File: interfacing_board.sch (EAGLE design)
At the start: 67 parts, among them IC1 MAX3096CSE, IC2 MAX3096CSE, X1 87758-3816, X2 87758-3816

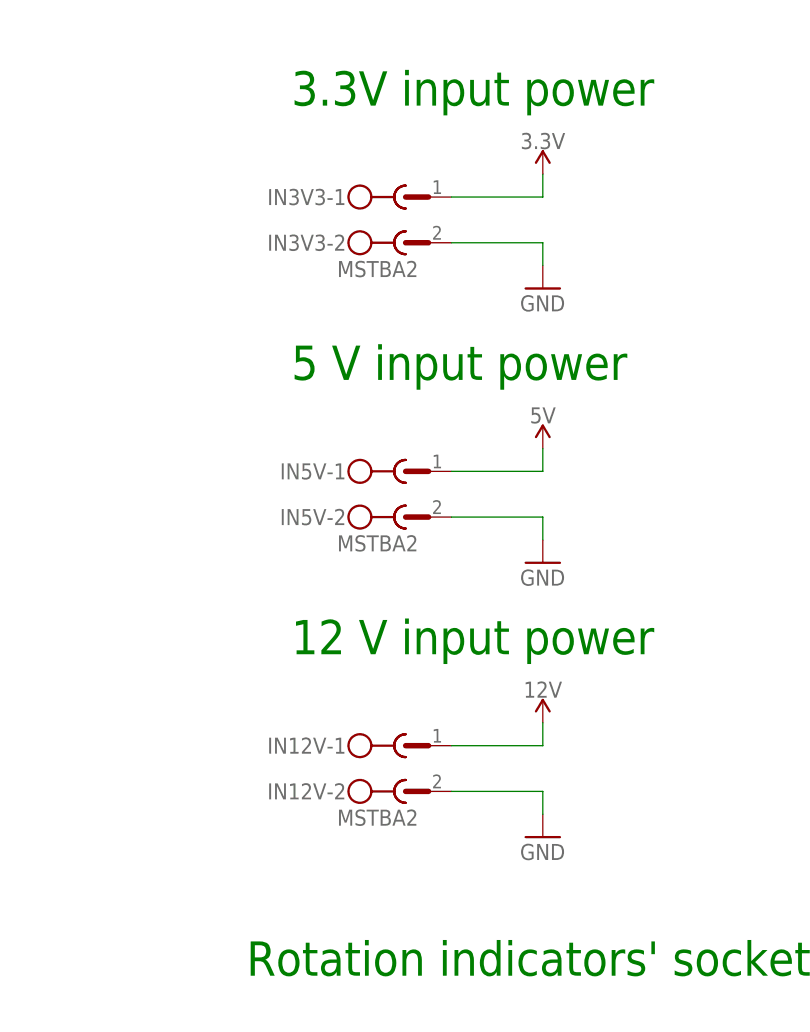
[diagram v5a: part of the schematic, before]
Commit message: Changed connector in bipop_power_supply board, modified routing and board's dimensions.
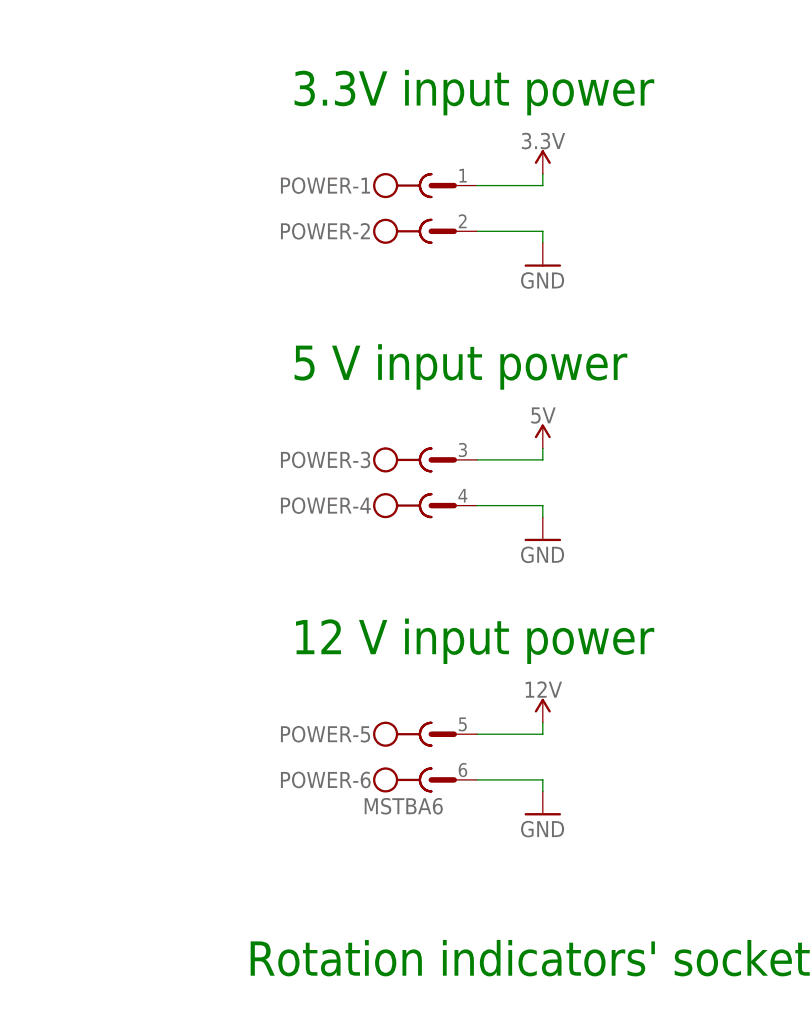
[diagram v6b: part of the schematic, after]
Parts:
- removed IN12V, IN3V3, IN5V: MSTBA2, con-phoenix-508:MSTBA2
- added POWER: MSTBA6, con-phoenix-508:MSTBA6
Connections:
- net 12V: now also POWER-5.1; no longer IN12V-1.1
- net 3.3V: now also POWER-1.1; no longer IN3V3-1.1
- net 5V: now also POWER-3.1; no longer IN5V-1.1
- net GND: now also POWER-2.1, POWER-4.1, POWER-6.1; no longer IN12V-2.1, IN3V3-2.1, IN5V-2.1
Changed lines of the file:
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@@
 <setting verticaltext="up"/>
 </settings>
-<grid distance="0.1" unitdist="inch" unit="inch" style="lines" multiple="1" display="no" altdistance="0.01" altunitdist="inch" altunit="inch"/>
+<grid distance="0.1" unitdist="inch" unit="inch" style="lines" multiple="1" display="yes" altdistance="0.01" altunitdist="inch" altunit="inch"/>
 <layers>
 <layer number="1" name="Top" color="4" fill="10" visible="no" active="no"/>
@@
 <part name="GND8" library="supply1" library_urn="urn:adsk.eagle:library:371" deviceset="GND" device=""/>
 <part name="ETHER" library="con-garry" library_urn="urn:adsk.eagle:library:147" deviceset="332-10" device="" package3d_urn="urn:adsk.eagle:package:6812/1"/>
-<part name="IN12V" library="con-phoenix-508" library_urn="urn:adsk.eagle:library:176" deviceset="MSTBA2" device="" package3d_urn="urn:adsk.eagle:package:9615/1"/>
-<part name="IN3V3" library="con-phoenix-508" library_urn="urn:adsk.eagle:library:176" deviceset="MSTBA2" device="" package3d_urn="urn:adsk.eagle:package:9615/1"/>
 <part name="GND21" library="supply1" library_urn="urn:adsk.eagle:library:371" deviceset="GND" device=""/>
 <part name="SUPPLY15" library="SparkFun-PowerSymbols" library_urn="urn:adsk.eagle:library:530" deviceset="12V" device=""/>
@@
 <part name="SUPPLY39" library="SparkFun-PowerSymbols" library_urn="urn:adsk.eagle:library:530" deviceset="3.3V" device=""/>
 <part name="GND4" library="supply1" library_urn="urn:adsk.eagle:library:371" deviceset="GND" device=""/>
-<part name="IN5V" library="con-phoenix-508" library_urn="urn:adsk.eagle:library:176" deviceset="MSTBA2" device="" package3d_urn="urn:adsk.eagle:package:9615/1"/>
 <part name="SUPPLY24" library="SparkFun-PowerSymbols" library_urn="urn:adsk.eagle:library:530" deviceset="3.3V" device=""/>
 <part name="GND39" library="supply1" library_urn="urn:adsk.eagle:library:371" deviceset="GND" device=""/>
@@
 <part name="GND31" library="SparkFun-PowerSymbols" library_urn="urn:adsk.eagle:library:530" deviceset="GND" device=""/>
 <part name="GND32" library="SparkFun-PowerSymbols" library_urn="urn:adsk.eagle:library:530" deviceset="GND" device=""/>
+<part name="POWER" library="con-phoenix-508" library_urn="urn:adsk.eagle:library:176" deviceset="MSTBA6" device="" package3d_urn="urn:adsk.eagle:package:9616/1"/>
 </parts>
 <sheets>
@@
 <instance part="X2" gate="-37" x="-18.44" y="179.42" rot="R180"/>
 <instance part="X2" gate="-38" x="-43.84" y="179.42" rot="MR180"/>
-<instance part="GND2" gate="1" x="-15.552978125" y="-118.11301875"/>
+<instance part="GND2" gate="1" x="-15.552978125" y="-115.57301875"/>
 <instance part="GND3" gate="1" x="63.027021875" y="-172.39301875"/>
 <instance part="SUPPLY2" gate="G$1" x="63.027021875" y="-164.69301875"/>
@@
 <instance part="ETHER" gate="-9" x="84.007021875" y="-122.59301875" rot="MR0"/>
 <instance part="ETHER" gate="-10" x="53.527021875" y="-122.59301875"/>
-<instance part="IN12V" gate="-1" x="-30.792978125" y="-168.91301875"/>
-<instance part="IN12V" gate="-2" x="-30.792978125" y="-173.99301875"/>
-<instance part="IN3V3" gate="-1" x="-30.792978125" y="-107.95301875"/>
-<instance part="IN3V3" gate="-2" x="-30.792978125" y="-113.03301875"/>
-<instance part="GND21" gate="1" x="-15.552978125" y="-179.07301875"/>
+<instance part="GND21" gate="1" x="-15.552978125" y="-176.53301875"/>
 <instance part="SUPPLY15" gate="G$1" x="-15.552978125" y="-166.37301875"/>
 <instance part="SUPPLY1" gate="G$1" x="-15.552978125" y="-105.41301875"/>
@@
 <instance part="R18" gate="G$1" x="82.528246875" y="-388.03574375" rot="R90"/>
 <instance part="SUPPLY39" gate="G$1" x="82.528246875" y="-382.95574375"/>
-<instance part="GND4" gate="1" x="-15.552978125" y="-148.59301875"/>
-<instance part="IN5V" gate="-1" x="-30.792978125" y="-138.43301875"/>
-<instance part="IN5V" gate="-2" x="-30.792978125" y="-143.51301875"/>
+<instance part="GND4" gate="1" x="-15.552978125" y="-146.05301875"/>
 <instance part="SUPPLY24" gate="G$1" x="52.048246875" y="-382.95574375"/>
 <instance part="GND39" gate="1" x="52.048246875" y="-403.27574375"/>
@@
 <instance part="GND31" gate="1" x="7.62" y="210.82"/>
 <instance part="GND32" gate="1" x="7.62" y="226.06"/>
+<instance part="POWER" gate="-1" x="-27.94" y="-106.68"/>
+<instance part="POWER" gate="-2" x="-27.94" y="-111.76"/>
+<instance part="POWER" gate="-3" x="-27.94" y="-137.16"/>
+<instance part="POWER" gate="-4" x="-27.94" y="-142.24"/>
+<instance part="POWER" gate="-5" x="-27.94" y="-167.64"/>
+<instance part="POWER" gate="-6" x="-27.94" y="-172.72"/>
 </instances>
 <busses>
@@
 <net name="GND" class="0">
 <segment>
-<pinref part="GND2" gate="1" pin="GND"/>
-<wire x1="-25.712978125" y1="-113.03301875" x2="-15.552978125" y2="-113.03301875" width="0.1524" layer="91"/>
-<wire x1="-15.552978125" y1="-113.03301875" x2="-15.552978125" y2="-115.57301875" width="0.1524" layer="91"/>
-<pinref part="IN3V3" gate="-2" pin="1"/>
-</segment>
-<segment>
 <pinref part="ETHER" gate="-10" pin="S"/>
 <wire x1="50.987021875" y1="-122.59301875" x2="48.447021875" y2="-122.59301875" width="0.1524" layer="91"/>
 <pinref part="GND8" gate="1" pin="GND"/>
 <wire x1="48.447021875" y1="-122.59301875" x2="48.447021875" y2="-125.13301875" width="0.1524" layer="91"/>
-</segment>
-<segment>
-<pinref part="IN12V" gate="-2" pin="1"/>
-<pinref part="GND21" gate="1" pin="GND"/>
-<wire x1="-25.712978125" y1="-173.99301875" x2="-15.552978125" y2="-173.99301875" width="0.1524" layer="91"/>
-<wire x1="-15.552978125" y1="-173.99301875" x2="-15.552978125" y2="-176.53301875" width="0.1524" layer="91"/>
-</segment>
-<segment>
-<pinref part="IN5V" gate="-2" pin="1"/>
-<pinref part="GND4" gate="1" pin="GND"/>
-<wire x1="-25.712978125" y1="-143.51301875" x2="-15.552978125" y2="-143.51301875" width="0.1524" layer="91"/>
-<wire x1="-15.552978125" y1="-143.51301875" x2="-15.552978125" y2="-146.05301875" width="0.1524" layer="91"/>
 </segment>
 <segment>
@@
 <wire x1="7.62" y1="230.22" x2="7.62" y2="228.6" width="0.1524" layer="91"/>
 </segment>
+<segment>
+<pinref part="GND2" gate="1" pin="GND"/>
+<pinref part="POWER" gate="-2" pin="1"/>
+<wire x1="-15.552978125" y1="-113.03301875" x2="-15.552978125" y2="-111.76" width="0.1524" layer="91"/>
+<wire x1="-15.552978125" y1="-111.76" x2="-22.86" y2="-111.76" width="0.1524" layer="91"/>
+</segment>
+<segment>
+<pinref part="GND4" gate="1" pin="GND"/>
+<pinref part="POWER" gate="-4" pin="1"/>
+<wire x1="-15.552978125" y1="-143.51301875" x2="-15.552978125" y2="-142.24" width="0.1524" layer="91"/>
+<wire x1="-15.552978125" y1="-142.24" x2="-22.86" y2="-142.24" width="0.1524" layer="91"/>
+</segment>
+<segment>
+<pinref part="GND21" gate="1" pin="GND"/>
+<pinref part="POWER" gate="-6" pin="1"/>
+<wire x1="-15.552978125" y1="-173.99301875" x2="-15.552978125" y2="-172.72" width="0.1524" layer="91"/>
+<wire x1="-15.552978125" y1="-172.72" x2="-22.86" y2="-172.72" width="0.1524" layer="91"/>
+</segment>
 </net>
 <net name="PA15" class="0">
@@
 </segment>
 <segment>
-<wire x1="-25.712978125" y1="-107.95301875" x2="-15.552978125" y2="-107.95301875" width="0.1524" layer="91"/>
-<wire x1="-15.552978125" y1="-107.95301875" x2="-15.552978125" y2="-105.41301875" width="0.1524" layer="91"/>
-<pinref part="IN3V3" gate="-1" pin="1"/>
-<pinref part="SUPPLY1" gate="G$1" pin="3.3V"/>
-</segment>
-<segment>
 <pinref part="R18" gate="G$1" pin="2"/>
 <pinref part="SUPPLY39" gate="G$1" pin="3.3V"/>
@@
 <pinref part="SUPPLY35" gate="G$1" pin="3.3V"/>
 </segment>
+<segment>
+<pinref part="SUPPLY1" gate="G$1" pin="3.3V"/>
+<pinref part="POWER" gate="-1" pin="1"/>
+<wire x1="-15.552978125" y1="-105.41301875" x2="-15.552978125" y2="-106.68" width="0.1524" layer="91"/>
+<wire x1="-15.552978125" y1="-106.68" x2="-22.86" y2="-106.68" width="0.1524" layer="91"/>
+</segment>
 </net>
 <net name="5V" class="0">
-<segment>
-<pinref part="IN5V" gate="-1" pin="1"/>
-<pinref part="SUPPLY5" gate="G$1" pin="5V"/>
-<wire x1="-25.712978125" y1="-138.43301875" x2="-15.552978125" y2="-138.43301875" width="0.1524" layer="91"/>
-<wire x1="-15.552978125" y1="-138.43301875" x2="-15.552978125" y2="-135.89301875" width="0.1524" layer="91"/>
-</segment>
 <segment>
 <pinref part="ENDR2" gate="-2" pin="S"/>
@@
 <wire x1="45.407021875" y1="29.20698125" x2="45.407021875" y2="25.4" width="0.1524" layer="91"/>
 </segment>
+<segment>
+<pinref part="SUPPLY5" gate="G$1" pin="5V"/>
+<pinref part="POWER" gate="-3" pin="1"/>
+<wire x1="-15.552978125" y1="-135.89301875" x2="-15.552978125" y2="-137.16" width="0.1524" layer="91"/>
+<wire x1="-15.552978125" y1="-137.16" x2="-22.86" y2="-137.16" width="0.1524" layer="91"/>
+</segment>
 </net>
 <net name="INT" class="0">
@@
 <wire x1="86.547021875" y1="-112.43301875" x2="89.087021875" y2="-112.43301875" width="0.1524" layer="91"/>
 <label x="89.087021875" y="-112.43301875" size="1.27" layer="95" rot="MR180" xref="yes"/>
-</segment>
-</net>
-<net name="12V" class="0">
-<segment>
-<pinref part="IN12V" gate="-1" pin="1"/>
-<pinref part="SUPPLY15" gate="G$1" pin="12V"/>
-<wire x1="-25.712978125" y1="-168.91301875" x2="-15.552978125" y2="-168.91301875" width="0.1524" layer="91"/>
-<wire x1="-15.552978125" y1="-168.91301875" x2="-15.552978125" y2="-166.37301875" width="0.1524" layer="91"/>
 </segment>
 </net>
@@
 </segment>
 </net>
+<net name="12V" class="0">
+<segment>
+<pinref part="SUPPLY15" gate="G$1" pin="12V"/>
+<pinref part="POWER" gate="-5" pin="1"/>
+<wire x1="-15.552978125" y1="-166.37301875" x2="-15.552978125" y2="-167.64" width="0.1524" layer="91"/>
+<wire x1="-15.552978125" y1="-167.64" x2="-22.86" y2="-167.64" width="0.1524" layer="91"/>
+</segment>
+</net>

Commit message: Circuit converted to single-periscope operation mode. Duplicate components removed.
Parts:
- removed DRIVER1-, DRIVER2-: DRV8871, SKA_EP_molex_6410_7395:DRV8871
- removed ENDR2: 332-10, con-garry:332-10
- removed IC2: MAX3096CSE, maxim:MAX3096CSE
- removed OPENLOG: OPENLOG, SKA_EP_molex_6410_7395:OPENLOG
- removed OPTO5, OPTO7: 332-04, con-garry:332-04
- removed R24, R29, R31: 5k, rcl:R-EU_M0805
- removed R25, R60, R61, R65, R66, R67: (no value), resistor:R-EU_M0805
- removed R26, R30, R32: 10k, rcl:R-EU_M0805
- removed UV2, VIS2: 22-05-7048-04, EP_molex_6410_7395:22-05-7048-04
- added DRV_: DRV8871, customy:DRV8871
- added SD: 22-23-2071, con-molex:22-23-2071
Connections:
- removed net CHA-2: IC2.Y1, R24.2
- removed net CHB-2: IC2.Y2, R29.2
- removed net CHB2-L: R29.1, R30.2
- removed net CHC-2: IC2.Y3, R31.2
- removed net DRV2-VM: DRIVER2-VM.1
- removed net INCHA-2: ENDR2-6.S, IC2.A1
- removed net INCHB-2: ENDR2-8.S, IC2.A2
- removed net INCHC-2: ENDR2-10.S, IC2.A3
- removed net IND3: OPTO5-1.S, R61.2
- removed net IND4: OPTO7-1.S, R67.2
- removed net N$11: OPTO5-4.S, R25.1
- removed net N$13: IC2.!G, R4.1
- removed net N$16: OPTO7-3.S, R66.1
- removed net N$23: OPTO7-4.S, R65.1
- removed net N$5: OPTO5-3.S, R60.1
- removed net N$8: IC2.G, R3.2
- removed net OL-BLK: OPENLOGBLK.1
- removed net OL-GRN: OPENLOGGRN.1
- removed net SCL2: VIS1-3.S, VIS2-3.S
- removed net SDA2: VIS1-2.S, VIS2-2.S
- removed net ~INCHA-2: ENDR2-5.S, IC2.B1
- removed net ~INCHB-2: ENDR2-7.S, IC2.B2
- removed net ~INCHC-2: ENDR2-9.S, IC2.B3
- new net CD_SD: SD-1.S
- net +5V: no longer R3.1
- net 12V: now also DRV_MOT_VCC.S
- net 3.3V: now also R3.2, R4.2, SD-6.S; no longer OPENLOGVCC.1, R25.2, R60.2, R65.2, R66.2, UV2-1.S, VIS2-1.S
- net 5V: no longer ENDR2-2.S, IC2.VCC
- net CHA-2L: no longer R24.1, R26.2
- net CHC-2L: no longer R31.1, R32.2
- net CS_SD: now also SD-2.S
- net DRV1-VM: now also DRV_VM.1; no longer DRIVER1-VM.1
- net GND: now also DRV_GND.1, DRV_MOT_GND.S, SD-7.S; no longer DRIVER1-GND.1, DRIVER2-GND.1, ENDR2-3.S, IC2.GND, OPENLOGGND.1, OPTO5-2.S, OPTO7-2.S, R26.1, R30.1, R32.1, R4.2, R61.1, R67.1, UV2-4.S, VIS2-4.S
- net M11: now also DRV_IN1.1, R4.1; no longer DRIVER1-IN1.1
- net M12: now also DRV_IN2.1, R3.1; no longer DRIVER1-IN2.1
- net M21: no longer DRIVER2-IN1.1
- net M22: no longer DRIVER2-IN2.1
- net OL_RX: no longer OPENLOGRXI.1
- net OL_TX: no longer OPENLOGTXO.1
- net SCL1: now also VIS1-3.S; no longer UV2-3.S
- net SDA1: now also VIS1-2.S; no longer UV2-2.S
- net SPI1_MISO: now also SD-4.S
- net SPI1_MOSI: now also SD-5.S
- net SPI1_SCK: now also SD-3.S
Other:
- note added: "23.06.2018"
- note added: "Encoders' socket"
- note added: "Motor's driver"
- note added: "RS-422 encoder receiver"
- note added: "Rev1.5"
- note added: "SD Card socket"
- note removed: "14.05.2018"
- note removed: "Encoders' sockets"
- note removed: "Motors' drivers"
- note removed: "RS-422 encoder receivers"
- note removed: "Rev1.4"
- note removed: "SD Card OpenLog socket"
- note removed: "connect missing pins to Nucleo"
- moved on the sheet: R3, R4, VIS1-1, VIS1-2, VIS1-3, VIS1-4

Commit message: Schematics reorganised to be more readable.
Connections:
- net CHA-2L renamed PA1
- net CHB-2L renamed PB10
- net CHC-2L renamed PB11
- net M21 renamed PA2
- net M22 renamed PA3
- net OL_RX renamed PA9
- net OL_TX renamed PA10
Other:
- moved on the sheet: ALBEDO1-1, ALBEDO1-2, ALBEDO1-3, ALBEDO1-4, ALBEDO2-1, ALBEDO2-2, ALBEDO2-3, ALBEDO2-4, DRV_GND, DRV_IN1, DRV_IN2, DRV_MOT_GND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
